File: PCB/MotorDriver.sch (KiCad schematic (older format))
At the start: 5 parts, among them U1 DRV8871DDA

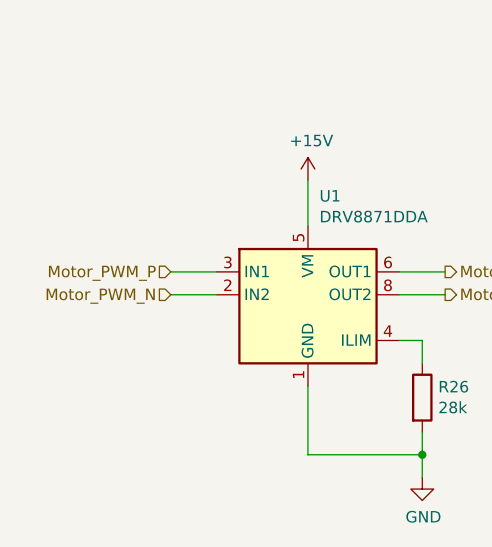
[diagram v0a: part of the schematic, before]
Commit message: Initial commit of the Quartus project
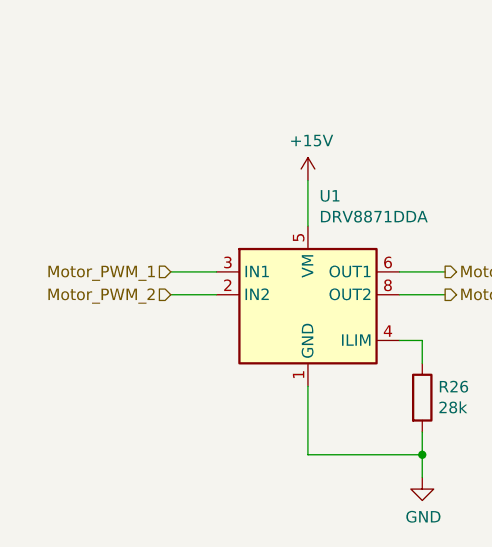
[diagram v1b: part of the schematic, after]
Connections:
- net Motor_PWM_N renamed Motor_PWM_2
- net Motor_PWM_P renamed Motor_PWM_1
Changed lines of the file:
@@
 Connection ~ 6000 2500
 Text HLabel 4900 4100 0    50   Input ~ 0
-Motor_PWM_P
+Motor_PWM_1
 Text HLabel 4900 4200 0    50   Input ~ 0
-Motor_PWM_N
+Motor_PWM_2
 Wire Wire Line
 	4900 4100 5100 4100

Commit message: Connect the FPGA configuration signals
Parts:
- C1, C2: Part_Number C3216X5R1E476M160AC -> (none); Part_number (none) -> C3216X5R1E476M160AC
- C3: Part_Number C1608X5R1H104K080AA -> (none); Part_number (none) -> C1608X5R1H104K080AA
- R26: Part_Number CR0603-FX-2802ELF -> (none); Part_number (none) -> CR0603-FX-2802ELF
- U1: Part_Number DRV8871DDARQ1 -> (none); Part_number (none) -> DRV8871DDARQ1
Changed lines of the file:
@@
 F 2 "Capacitor_SMD:C_0603_1608Metric" H 6038 2100 50  0001 C CNN
 F 3 "~" H 6000 2250 50  0001 C CNN
-F 4 "C1608X5R1H104K080AA" H 6000 2250 50  0001 C CNN "Part_Number"
+F 4 "" H 6000 2250 50  0001 C CNN "Part_Number"
 F 5 "50V" H 6115 2159 50  0000 L CNN "Voltage"
+F 6 "C1608X5R1H104K080AA" H 6000 2250 50  0001 C CNN "Part_number"
 	1    6000 2250
 	1    0    0    -1
@@
 F 2 "Capacitor_SMD:C_0603_1608Metric" H 5038 2100 50  0001 C CNN
 F 3 "~" H 5000 2250 50  0001 C CNN
-F 4 "C3216X5R1E476M160AC" H 5000 2250 50  0001 C CNN "Part_Number"
+F 4 "" H 5000 2250 50  0001 C CNN "Part_Number"
 F 5 "25V" H 5115 2159 50  0000 L CNN "Voltage"
+F 6 "C3216X5R1E476M160AC" H 5000 2250 50  0001 C CNN "Part_number"
 	1    5000 2250
 	1    0    0    -1
@@
 F 2 "Capacitor_SMD:C_0603_1608Metric" H 5538 2100 50  0001 C CNN
 F 3 "~" H 5500 2250 50  0001 C CNN
-F 4 "C3216X5R1E476M160AC" H 5500 2250 50  0001 C CNN "Part_Number"
+F 4 "" H 5500 2250 50  0001 C CNN "Part_Number"
 F 5 "25V" H 5615 2159 50  0000 L CNN "Voltage"
+F 6 "C3216X5R1E476M160AC" H 5500 2250 50  0001 C CNN "Part_number"
 	1    5500 2250
 	1    0    0    -1
@@
 F 1 "28k" H 6070 4605 50  0000 L CNN
 F 2 "Resistor_SMD:R_0603_1608Metric" V 5930 4650 50  0001 C CNN
-F 3 "~" H 6000 4650 50  0001 C CNN
-F 4 "CR0603-FX-2802ELF" H 6000 4650 50  0001 C CNN "Part_Number"
+F 3 "https://www.bourns.com/docs/product-datasheets/CRxxxxx.pdf" H 6000 4650 50  0001 C CNN
+F 4 "" H 6000 4650 50  0001 C CNN "Part_Number"
+F 5 "CR0603-FX-2802ELF" H 6000 4650 50  0001 C CNN "Part_number"
 	1    6000 4650
 	1    0    0    -1
@@
 F 2 "Package_SO:Texas_HTSOP-8-1EP_3.9x4.9mm_P1.27mm_EP2.95x4.9mm_Mask2.4x3.1mm_ThermalVias" H 5750 4150 50  0001 C CNN
 F 3 "http://www.ti.com/lit/ds/symlink/drv8871.pdf" H 5750 4150 50  0001 C CNN
-F 4 "DRV8871DDARQ1" H 5500 4200 50  0001 C CNN "Part_Number"
+F 4 "" H 5500 4200 50  0001 C CNN "Part_Number"
+F 5 "DRV8871DDARQ1" H 5500 4200 50  0001 C CNN "Part_number"
 	1    5500 4200
 	1    0    0    -1
